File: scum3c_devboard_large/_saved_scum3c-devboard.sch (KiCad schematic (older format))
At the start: 34 parts, among them J1 CONSMA001-SMD-G-T, J10 Conn_01x02, J11 Conn_01x01, J3 Conn_02x06_Odd_Even, J5 Conn_02x04_Odd_Even, J6 Conn_01x03, J7 Conn_01x03, J8 Conn_01x03, U1 Perfboard, U12 S-85S1AB18-I6T1U, U5 ICM-20948, U6 S-85S1AB10-I6T1U, U7 S-85S1AB15-I6T1U

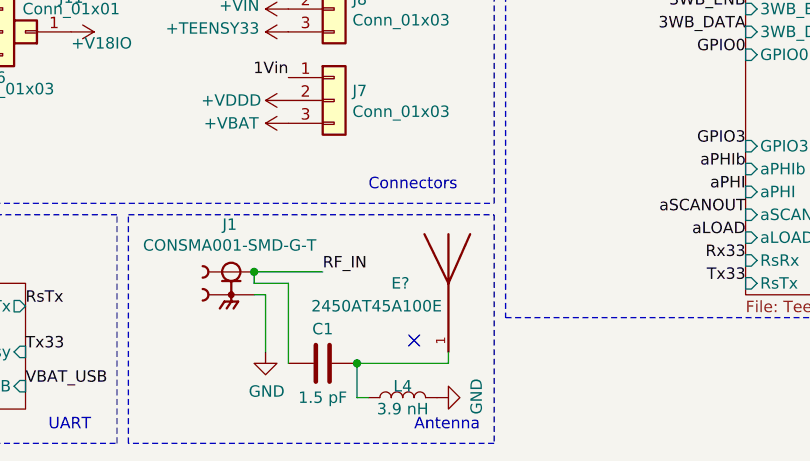
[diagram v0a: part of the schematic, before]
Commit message: Added images
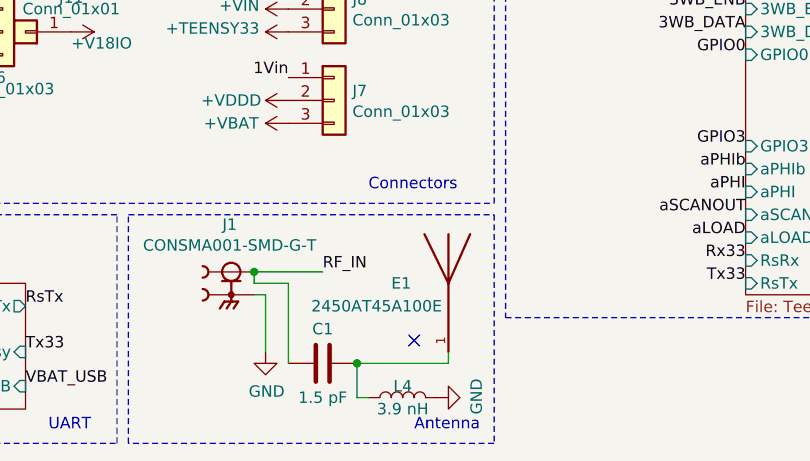
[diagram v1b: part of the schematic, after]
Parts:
- gave numbers to parts that had none: 1
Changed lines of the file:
@@
 Connection ~ 3100 1700
 $Comp
-L 2450AT45A100E:2450AT45A100E E?
+L 2450AT45A100E:2450AT45A100E E1
 U 1 1 6011A2BA
 P 3250 7200
-F 0 "E?" H 3000 7300 50  0000 L CNN
+F 0 "E1" H 3000 7300 50  0000 L CNN
 F 1 "2450AT45A100E" H 2650 7200 50  0000 L CNN
 F 2 "ANT_2450AT45A100E" H 3250 7200 50  0001 L BNN
